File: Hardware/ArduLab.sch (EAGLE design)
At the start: 91 parts, among them CN1 USB-B, CN2 JST-PH, Q1 BSS138, Q2 BSS138, U1 ATMEGA32U4-AU, U2 MIC5205, U3 PAM2401, U4 MCP73831, U5 L293DD, X1 16MHz

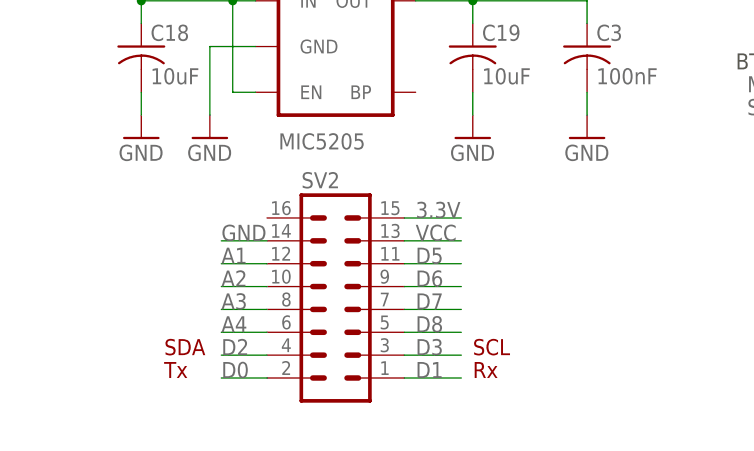
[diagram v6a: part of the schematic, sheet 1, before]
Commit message: Updated Mod Interface for RadioLab compatibility
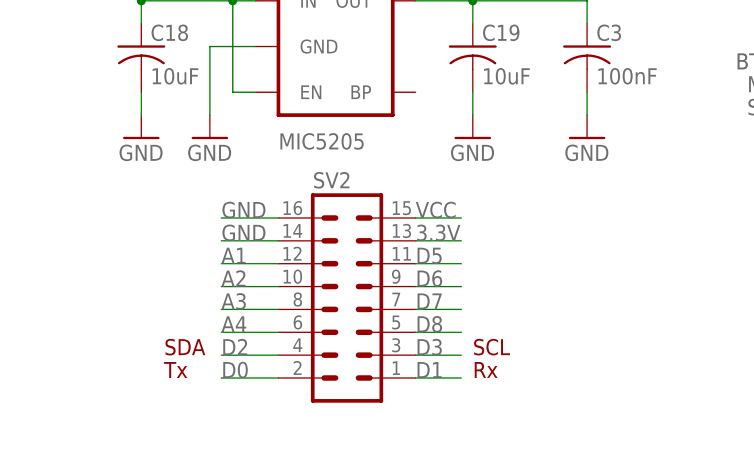
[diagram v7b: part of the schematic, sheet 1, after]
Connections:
- net 3.3V: now also SV2.13; no longer SV2.15
- net GND: now also SV2.16
- net VCC: now also SV2.15; no longer SV2.13
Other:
- moved on the sheet: SV2
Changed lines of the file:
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@@
 <instance part="GND42" gate="1" x="236.22" y="62.23"/>
 <instance part="P+7" gate="G$1" x="185.42" y="77.47"/>
-<instance part="SV2" gate="G$1" x="46.99" y="17.78"/>
+<instance part="SV2" gate="G$1" x="48.26" y="17.78"/>
 </instances>
 <busses>
@@
 </segment>
 <segment>
-<wire x1="39.37" y1="25.4" x2="34.29" y2="25.4" width="0.1524" layer="91"/>
+<wire x1="40.64" y1="25.4" x2="34.29" y2="25.4" width="0.1524" layer="91"/>
 <label x="34.29" y="25.4" size="1.778" layer="95"/>
 <pinref part="SV2" gate="G$1" pin="14"/>
+</segment>
+<segment>
+<wire x1="40.64" y1="27.94" x2="34.29" y2="27.94" width="0.1524" layer="91"/>
+<label x="34.29" y="27.94" size="1.778" layer="95"/>
+<pinref part="SV2" gate="G$1" pin="16"/>
 </segment>
 </net>
@@
 </segment>
 <segment>
-<wire x1="54.61" y1="25.4" x2="60.96" y2="25.4" width="0.1524" layer="91"/>
-<label x="55.88" y="25.4" size="1.778" layer="95"/>
-<pinref part="SV2" gate="G$1" pin="13"/>
+<wire x1="55.88" y1="27.94" x2="60.96" y2="27.94" width="0.1524" layer="91"/>
+<label x="55.88" y="27.94" size="1.778" layer="95"/>
+<pinref part="SV2" gate="G$1" pin="15"/>
 </segment>
 </net>
@@
 </segment>
 <segment>
-<wire x1="39.37" y1="12.7" x2="34.29" y2="12.7" width="0.1524" layer="91"/>
+<wire x1="40.64" y1="12.7" x2="34.29" y2="12.7" width="0.1524" layer="91"/>
 <label x="34.29" y="12.7" size="1.778" layer="95"/>
 <pinref part="SV2" gate="G$1" pin="4"/>
@@
 </segment>
 <segment>
-<wire x1="34.29" y1="22.86" x2="39.37" y2="22.86" width="0.1524" layer="91"/>
+<wire x1="34.29" y1="22.86" x2="40.64" y2="22.86" width="0.1524" layer="91"/>
 <label x="34.29" y="22.86" size="1.778" layer="95"/>
 <pinref part="SV2" gate="G$1" pin="12"/>
@@
 </segment>
 <segment>
-<wire x1="39.37" y1="20.32" x2="34.29" y2="20.32" width="0.1524" layer="91"/>
+<wire x1="40.64" y1="20.32" x2="34.29" y2="20.32" width="0.1524" layer="91"/>
 <label x="34.29" y="20.32" size="1.778" layer="95"/>
 <pinref part="SV2" gate="G$1" pin="10"/>
@@
 </segment>
 <segment>
-<wire x1="34.29" y1="17.78" x2="39.37" y2="17.78" width="0.1524" layer="91"/>
+<wire x1="34.29" y1="17.78" x2="40.64" y2="17.78" width="0.1524" layer="91"/>
 <label x="34.29" y="17.78" size="1.778" layer="95"/>
 <pinref part="SV2" gate="G$1" pin="8"/>
@@
 </segment>
 <segment>
-<wire x1="54.61" y1="12.7" x2="60.96" y2="12.7" width="0.1524" layer="91"/>
+<wire x1="55.88" y1="12.7" x2="60.96" y2="12.7" width="0.1524" layer="91"/>
 <label x="55.88" y="12.7" size="1.778" layer="95"/>
 <pinref part="SV2" gate="G$1" pin="3"/>
@@
 </segment>
 <segment>
-<wire x1="60.96" y1="22.86" x2="54.61" y2="22.86" width="0.1524" layer="91"/>
+<wire x1="60.96" y1="22.86" x2="55.88" y2="22.86" width="0.1524" layer="91"/>
 <label x="55.88" y="22.86" size="1.778" layer="95"/>
 <pinref part="SV2" gate="G$1" pin="11"/>
@@
 </segment>
 <segment>
-<wire x1="54.61" y1="20.32" x2="60.96" y2="20.32" width="0.1524" layer="91"/>
+<wire x1="55.88" y1="20.32" x2="60.96" y2="20.32" width="0.1524" layer="91"/>
 <label x="55.88" y="20.32" size="1.778" layer="95"/>
 <pinref part="SV2" gate="G$1" pin="9"/>
@@
 </segment>
 <segment>
-<wire x1="54.61" y1="15.24" x2="60.96" y2="15.24" width="0.1524" layer="91"/>
+<wire x1="55.88" y1="15.24" x2="60.96" y2="15.24" width="0.1524" layer="91"/>
 <label x="55.88" y="15.24" size="1.778" layer="95"/>
 <pinref part="SV2" gate="G$1" pin="5"/>
@@
 </segment>
 <segment>
-<wire x1="54.61" y1="10.16" x2="60.96" y2="10.16" width="0.1524" layer="91"/>
+<wire x1="55.88" y1="10.16" x2="60.96" y2="10.16" width="0.1524" layer="91"/>
 <label x="55.88" y="10.16" size="1.778" layer="95"/>
 <pinref part="SV2" gate="G$1" pin="1"/>
@@
 </segment>
 <segment>
-<wire x1="39.37" y1="15.24" x2="34.29" y2="15.24" width="0.1524" layer="91"/>
+<wire x1="40.64" y1="15.24" x2="34.29" y2="15.24" width="0.1524" layer="91"/>
 <label x="34.29" y="15.24" size="1.778" layer="95"/>
 <pinref part="SV2" gate="G$1" pin="6"/>
@@
 </segment>
 <segment>
-<wire x1="60.96" y1="17.78" x2="54.61" y2="17.78" width="0.1524" layer="91"/>
+<wire x1="60.96" y1="17.78" x2="55.88" y2="17.78" width="0.1524" layer="91"/>
 <label x="55.88" y="17.78" size="1.778" layer="95"/>
 <pinref part="SV2" gate="G$1" pin="7"/>
@@
 </segment>
 <segment>
-<wire x1="39.37" y1="10.16" x2="34.29" y2="10.16" width="0.1524" layer="91"/>
+<wire x1="40.64" y1="10.16" x2="34.29" y2="10.16" width="0.1524" layer="91"/>
 <label x="34.29" y="10.16" size="1.778" layer="95"/>
 <pinref part="SV2" gate="G$1" pin="2"/>
@@
 </segment>
 <segment>
-<wire x1="54.61" y1="27.94" x2="60.96" y2="27.94" width="0.1524" layer="91"/>
-<label x="55.88" y="27.94" size="1.778" layer="95"/>
-<pinref part="SV2" gate="G$1" pin="15"/>
-</segment>
-</net>
+<wire x1="55.88" y1="25.4" x2="60.96" y2="25.4" width="0.1524" layer="91"/>
+<label x="55.88" y="25.4" size="1.778" layer="95"/>
+<pinref part="SV2" gate="G$1" pin="13"/>
+</segment>
+</net>

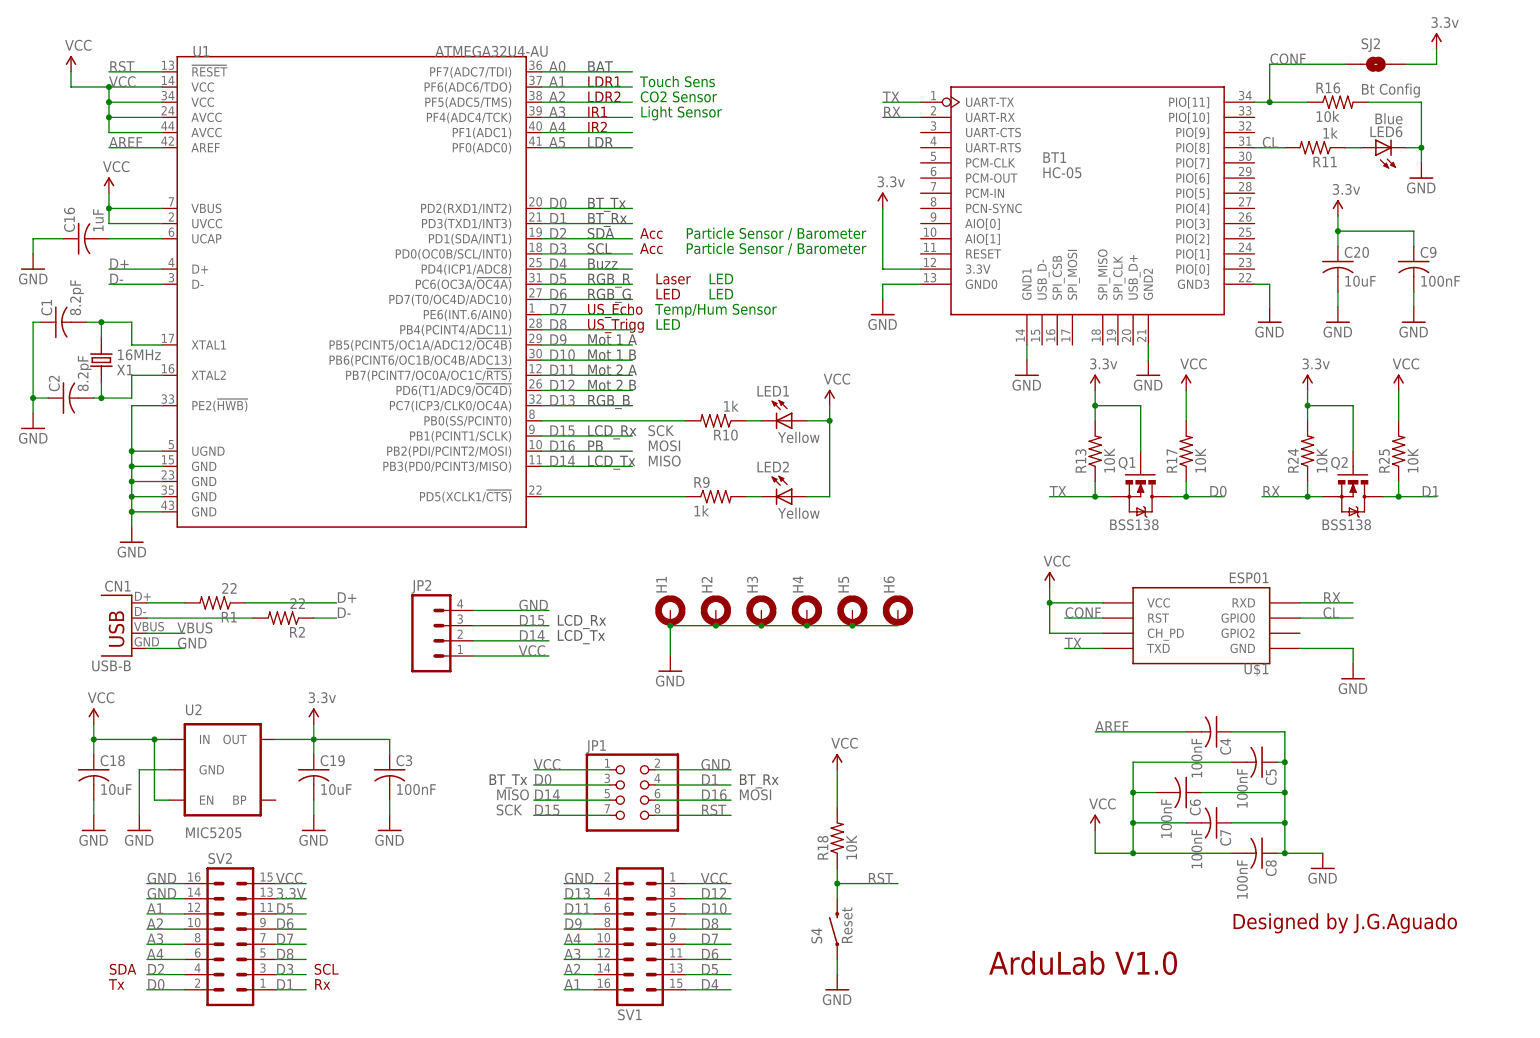
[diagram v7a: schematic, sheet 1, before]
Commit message: SCH and BRD updated. Added Production files (GERBER, BOM and CENTROID)
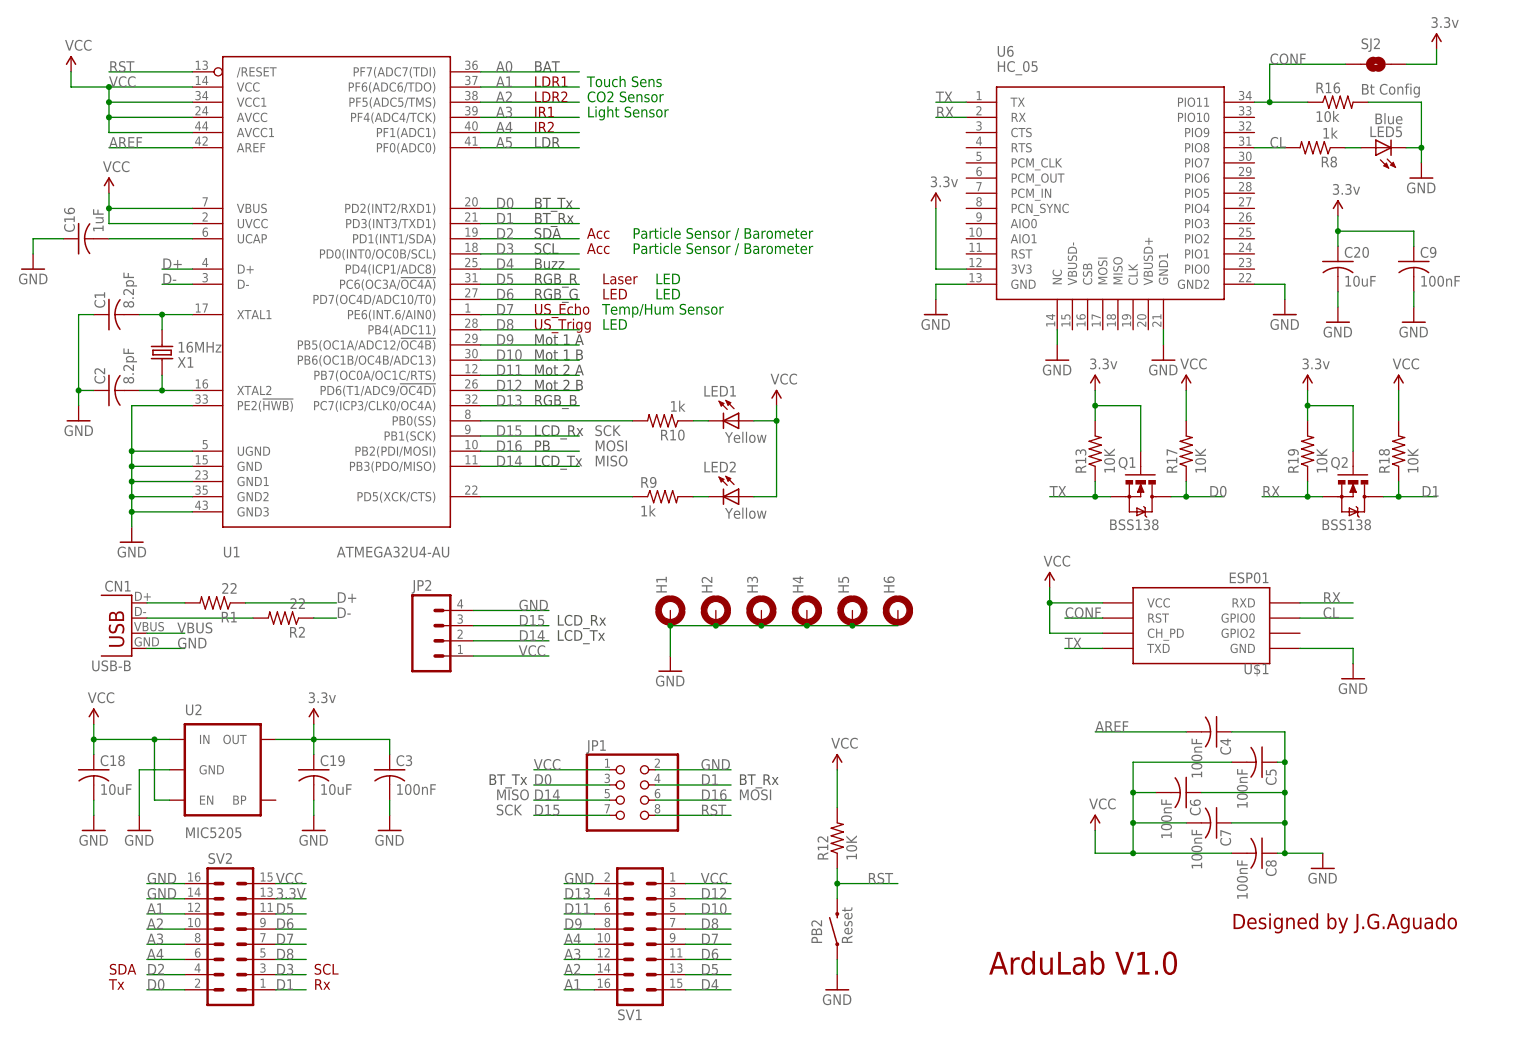
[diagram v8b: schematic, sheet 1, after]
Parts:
- removed BT1: HC-05, Module:BLUETOOTH-SERIALSMD
- removed R25: 10K, resistor:R-US_R1206
- added D3: MBR120, diode:DIODE-SOD123
- added R22: 750K, resistor:R-US_R1206
- added U6: HC_05, Bluetooth HC-05:HC_05
- R11: value 1k -> 2k
- R12: value 2k -> 10K
- R20: value 470 -> 100k
- R6: value 750K -> 330
- R7: value 100k -> 470
- R8: value 330 -> 1k
- U1: device IC:ATMEGA32U4-AU -> adafruit:ATMEGA32U4-AU
- renumbered LED6 to LED5, R24 to R19, S3 to PB1, S4 to PB2, X2 to CN3
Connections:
- new net N$3: D3.A, S1.RC
- net 3.3V: now also U6.3V3; no longer BT1.3.3V
- net A0: now also U1.PF7(ADC7(TDI); no longer U1.PF7(ADC7/TDI)
- net CL: now also R8.2, U6.PIO8; no longer BT1.PIO[8], R11.2
- net CONF: now also U6.PIO11; no longer BT1.PIO[11]
- net D0: now also U1.PD2(INT2/RXD1); no longer U1.PD2(RXD1/INT2)
- net D1: now also R18.1, U1.PD3(INT3/TXD1); no longer R25.1, U1.PD3(TXD1/INT3)
- net D10: now also U1.PB6(OC1B/OC4B/ADC13); no longer U1.PB6(PCINT6/OC1B/OC4B/ADC13)
- net D11: now also U1.PB7(OC0A/OC1C/RTS); no longer U1.PB7(PCINT7/OC0A/OC1C/!RTS)
- net D14: now also U1.PB3(PDO/MISO); no longer U1.PB3(PD0/PCINT3/MISO)
- net D15: now also U1.PB1(SCK); no longer U1.PB1(PCINT1/SCLK)
- net D16: now also U1.PB2(PDI/MOSI); no longer U1.PB2(PDI/PCINT2/MOSI)
- net D17/PB0/RXLED: now also U1.PB0(SS); no longer U1.PB0(SS/PCINT0)
- net D2: now also U1.PD1(INT1/SDA); no longer U1.PD1(SDA/INT1)
- net D3: now also U1.PD0(INT0/OC0B/SCL); no longer U1.PD0(OC0B/SCL/INT0)
- net D6: now also U1.PD7(OC4D/ADC10/T0); no longer U1.PD7(T0/OC4D/ADC10)
- net D8: now also U1.PB4(ADC11); no longer U1.PB4(PCINT4/ADC11)
- net D9: now also U1.PB5(OC1A/ADC12/!OC4B); no longer U1.PB5(PCINT5/OC1A/ADC12/!OC4B)
- net GND: now also R11.1, R20.2, R7.1, U1.GND, U1.GND1, U1.GND2, U1.GND3, U6.GND, U6.GND1, U6.GND2, U6.NC; no longer BT1.GND0, BT1.GND1, BT1.GND2, BT1.GND3, R12.1, R20.1, R7.2, U1.GND@1, U1.GND@2, U1.GND@3, U1.GND@4
- net N$1: now also R20.1, R22.1; no longer R6.1, R7.1
- net N$10: now also R11.2; no longer R12.2
- net N$11: now also R6.1; no longer R8.1
- net N$14: now also R7.2; no longer R20.2
- net N$19: now also R8.1; no longer R11.1
- net N$9: now also R6.2; no longer R8.2
- net PD5/TXLED: now also U1.PD5(XCK/CTS); no longer U1.PD5(XCLK1/!CTS)
- net RST: now also R12.1, U1./RESET; no longer R18.1, U1.!RESET
- net RX: now also U6.RX; no longer BT1.UART-RX
- net TX: now also U6.TX; no longer BT1.UART-TX
- net VCC: now also D3.C, R12.2, U1.AVCC, U1.AVCC1, U1.VCC, U1.VCC1; no longer R25.2, S1.RC, U1.AVCC@1, U1.AVCC@2, U1.VCC@1, U1.VCC@2
- net VOUT: now also R22.2; no longer R6.2
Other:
- moved on the sheet: C1, C2, LED1, LED2, LED3, R10, R18, R20, R6, R7, R9, X1
